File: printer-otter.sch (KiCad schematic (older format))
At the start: 52 parts, among them J1 12401610E4-2A, J3 OLED_64x32, P1 TC2030-CTX, SW1 Down, SW2 Setup, SW3 Up, U1 MT3608, U2 STM32F072C8Ux, U3 AP2204R-3.3, U4 USBLC6-4SC6, U5 L78L09_SOT89

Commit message: added connectors and board file
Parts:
- added J2: Conn_01x16, otter:Generic_FPC_0.5mm_15pin, symbol Connector_Generic:Conn_01x16
- added J4, J? (x3): Conn_01x06, Connector_Molex:Molex_PicoBlade_53261-0571_1x05-1MP_P1.25mm_Horizontal, symbol Connector_Generic:Conn_01x06
- added Q1, Q3: Q_NMOS_GSD, Package_TO_SOT_SMD:SOT-23, symbol Device:Q_NMOS_GSD
- added Q2, Q4: Q_PMOS_GSD, Package_TO_SOT_SMD:SOT-23, symbol Device:Q_PMOS_GSD
- added R11, R12, R13, R6, R7, R8: 2k, Resistor_SMD:R_0402_1005Metric, symbol Device:R
- C1, C19: value 1.0μF 25V -> 1uF; footprint Capacitor_SMD:C_0603_1608Metric -> Capacitor_SMD:C_0402_1005Metric
- C11, C9: value 1μF -> 1uF; footprint Capacitor_SMD:C_0603_1608Metric -> Capacitor_SMD:C_0402_1005Metric
- C2: value 2.2μF -> 1uF; footprint Capacitor_SMD:C_0603_1608Metric -> Capacitor_SMD:C_0402_1005Metric
- C3: value 1.0μF 25V -> 0.1μF; footprint Capacitor_SMD:C_0603_1608Metric -> Capacitor_SMD:C_0402_1005Metric
- C7: value 0.1μF -> 1uF
- D2: renamed from D?; footprint (none) -> Diode_SMD:D_SMB
- J3: footprint Connector_Harwin:Harwin_M20-89014xx_1x14_P2.54mm_Horizontal -> otter:0.69OLED
- L1: footprint (none) -> Inductor_SMD:L_Taiyo-Yuden_MD-4040
- P1: footprint Tag-Connect:TC2030-NL_SMALL -> Connector:Tag-Connect_TC2030-IDC-NL_2x03_P1.27mm_Vertical
- R15, R17: value 2kΩ -> 2k
- R4, R5: footprint (none) -> Resistor_SMD:R_0402_1005Metric
- U1: footprint (none) -> Package_TO_SOT_SMD:SOT-23-6
- U4: value USBLC6-4SC6 -> USBLC6-2SC6
- U6, U7: renamed from U?; footprint (none) -> Package_SO:SOIC-16W_5.3x10.2mm_P1.27mm
- gave numbers to parts that had none: 4
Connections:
- net labels added: +3.3V, DCLK, DCLK_HV, F3_HV, F5_HV
- net labels removed: CC1, CC2, DCLCK, S6_HV
- wire segments 161 -> 182
- no-connect marks 10 -> 13
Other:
- moved on the sheet: C10, C12, C13, C14, C15, C16, C17, C18, C20, C4, C5, C6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

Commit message: updated schematic, removed display and tag connect, routed board (80%)
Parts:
- removed C10, C12, C17, C3, C8: 0.1μF, Capacitor_SMD:C_0402_1005Metric, symbol Device:C
- removed C13, C14, C15, C16, C9: 1uF, Capacitor_SMD:C_0402_1005Metric, symbol Device:C
- removed J1: 12401610E4-2A, Connector_USB:USB_C_Receptacle_Amphenol_12401548E4-2A, symbol Connector:USB_C_Receptacle
- removed J3: OLED_64x32, otter:0.69OLED, symbol Connector_Generic:Conn_01x14
- removed J4, J? (x3): Conn_01x06, Connector_Molex:Molex_PicoBlade_53261-0571_1x05-1MP_P1.25mm_Horizontal, symbol Connector_Generic:Conn_01x06
- removed P1: TC2030-CTX, Connector:Tag-Connect_TC2030-IDC-NL_2x03_P1.27mm_Vertical, symbol Connector_Generic:Conn_02x03_Counter_Clockwise
- removed R15, R17: 2k, Resistor_SMD:R_0402_1005Metric, symbol Device:R
- removed R16: 560k, Resistor_SMD:R_0402_1005Metric, symbol Device:R_Small
- removed SW2: Setup, Button_Switch_SMD:SW_SPST_EVQP7C, symbol Switch:SW_Push
- removed SW3: Up, Button_Switch_SMD:SW_SPST_EVQP7C, symbol Switch:SW_Push
- added J1: USB, badgelib:USB-C 16Pin, symbol Connector:USB_C_Receptacle_USB2.0
- added J4: Encoder, Connector_PinHeader_2.54mm:PinHeader_1x05_P2.54mm_Vertical, symbol Connector_Generic:Conn_01x05
- added J5: UART, Connector_PinHeader_2.54mm:PinHeader_1x05_P2.54mm_Vertical, symbol Connector_Generic:Conn_01x05
- added J6: Analog, Connector_PinHeader_2.54mm:PinHeader_1x05_P2.54mm_Vertical, symbol Connector_Generic:Conn_01x05
- D2: footprint Diode_SMD:D_SMB -> Diode_SMD:D_SOD-123
- J2: value Conn_01x16 -> Printer
- U4: value USBLC6-2SC6 -> USBLC6-4SC6
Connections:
- net labels removed: INPUT0, INPUT1, INPUT2
- wire segments 182 -> 128
- no-connect marks 13 -> 4
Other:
- moved on the sheet: C11, C7, D1, D4, R1, R10, R3, R9

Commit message: schematic cleanup
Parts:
- U6, U7: footprint Package_SO:SOIC-16W_5.3x10.2mm_P1.27mm -> Package_SO:SOIC-16_3.9x9.9mm_P1.27mm
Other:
- moved on the sheet: C1, C11, C18, C19, C2, C20, C4, C5, C6, C7, D2, J1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

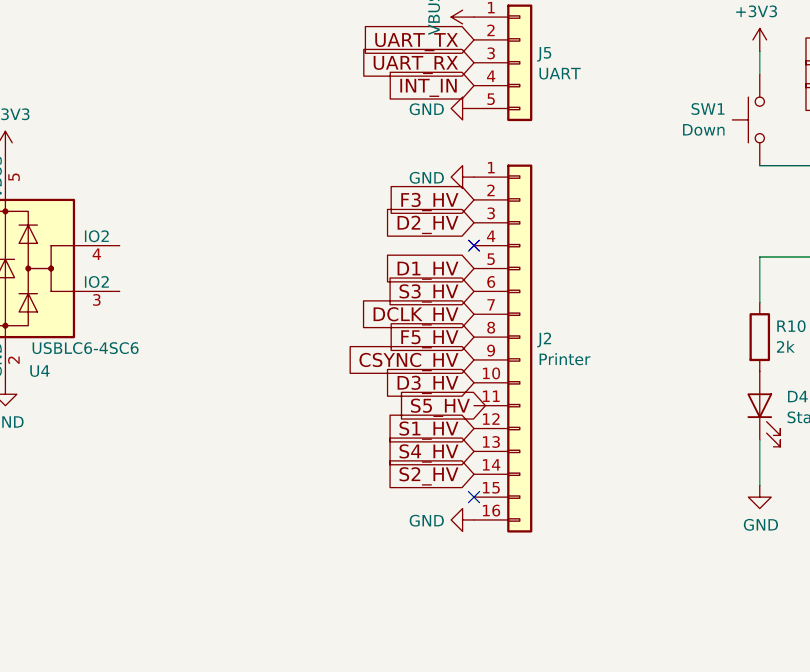
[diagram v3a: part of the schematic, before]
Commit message: fixed FPC pinout
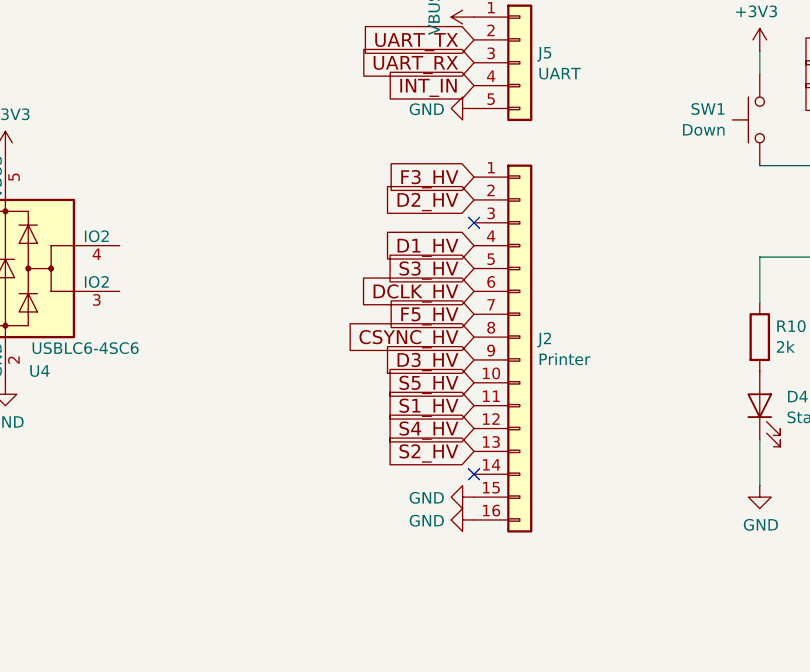
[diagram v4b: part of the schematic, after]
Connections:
- net CSYNC_HV: now also J2.8 (Pin_8); no longer J2.9 (Pin_9)
- net D1_HV: now also J2.4 (Pin_4); no longer J2.5 (Pin_5)
- net D2_HV: now also J2.2 (Pin_2); no longer J2.3 (Pin_3)
- net D3_HV: now also J2.9 (Pin_9); no longer J2.10 (Pin_10)
- net DCLK_HV: now also J2.6 (Pin_6); no longer J2.7 (Pin_7)
- net F3_HV: now also J2.1 (Pin_1); no longer J2.2 (Pin_2)
- net F5_HV: now also J2.7 (Pin_7); no longer J2.8 (Pin_8)
- net GND: now also J2.15 (Pin_15); no longer J2.1 (Pin_1)
- net S1_HV: now also J2.11 (Pin_11); no longer J2.12 (Pin_12)
- net S2_HV: now also J2.13 (Pin_13); no longer J2.14 (Pin_14)
- net S3_HV: now also J2.5 (Pin_5); no longer J2.6 (Pin_6)
- net S4_HV: now also J2.12 (Pin_12); no longer J2.13 (Pin_13)
- net S5_HV: now also J2.10 (Pin_10)
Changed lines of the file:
@@
 Text GLabel 12600 1650 3    60   Input ~ 0
 F5_HV
+Text GLabel 4250 5700 0    60   Input ~ 0
+S1_HV
+Text GLabel 4250 5900 0    60   Input ~ 0
+S2_HV
+Text GLabel 4250 5100 0    60   Input ~ 0
+S3_HV
 Text GLabel 4250 5800 0    60   Input ~ 0
-S1_HV
-Text GLabel 4250 6000 0    60   Input ~ 0
-S2_HV
+S4_HV
+Text GLabel 4250 5600 0    60   Input ~ 0
+S5_HV
 Text GLabel 4250 5200 0    60   Input ~ 0
-S3_HV
-Text GLabel 4250 5900 0    60   Input ~ 0
-S4_HV
-Text GLabel 4300 5700 0    60   Input ~ 0
-S5_HV
-Text GLabel 4250 5300 0    60   Input ~ 0
 DCLK_HV
-Text GLabel 4250 5100 0    60   Input ~ 0
+Text GLabel 4250 5000 0    60   Input ~ 0
 D1_HV
-Text GLabel 4250 4900 0    60   Input ~ 0
+Text GLabel 4250 4800 0    60   Input ~ 0
 D2_HV
-Text GLabel 4250 5600 0    60   Input ~ 0
+Text GLabel 4250 5500 0    60   Input ~ 0
 D3_HV
-Text GLabel 4250 5500 0    60   Input ~ 0
+Text GLabel 4250 5400 0    60   Input ~ 0
 CSYNC_HV
 $Comp
 L power:GND #PWR0155
 U 1 1 5C893C32
-P 4250 4700
-F 0 "#PWR0155" H 4250 4450 50  0001 C CNN
-F 1 "GND" V 4255 4572 50  0000 R CNN
-F 2 "" H 4250 4700 50  0001 C CNN
-F 3 "" H 4250 4700 50  0001 C CNN
-	1    4250 4700
+P 4250 6100
+F 0 "#PWR0155" H 4250 5850 50  0001 C CNN
+F 1 "GND" V 4255 5972 50  0000 R CNN
+F 2 "" H 4250 6100 50  0001 C CNN
+F 3 "" H 4250 6100 50  0001 C CNN
+	1    4250 6100
 	0    1    1    0
 $EndComp
-Text GLabel 4250 5400 0    60   Input ~ 0
+Text GLabel 4250 5300 0    60   Input ~ 0
 F5_HV
-Text GLabel 4250 4800 0    60   Input ~ 0
+Text GLabel 4250 4700 0    60   Input ~ 0
 F3_HV
-NoConn ~ 4250 5000
-NoConn ~ 4250 6100
+NoConn ~ 4250 4900
+NoConn ~ 4250 6000
 $Comp
 L Device:C C?

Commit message: updated kicad files
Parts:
- removed C19: 1uF, Capacitor_SMD:C_0402_1005Metric, symbol Device:C
- removed JP1: Boot, Jumper:SolderJumper-2_P1.3mm_Open_RoundedPad1.0x1.5mm, symbol Jumper:SolderJumper_2_Open
- added C3: 10µF, Capacitor_SMD:CP_Elec_4x3, symbol Device:CP1
- C1, C18, C2, C21, C22, C23, C24, C4, C5, C6, C7: footprint Capacitor_SMD:C_0402_1005Metric -> Capacitor_SMD:C_0603_1608Metric
- C11, C20: footprint Capacitor_SMD:C_0402_1005Metric -> Capacitor_SMD:C_0805_2012Metric
- R1, R10, R11, R12, R13, R2, R3, R4, R5, R6, R7, R8, R9: footprint Resistor_SMD:R_0402_1005Metric -> Resistor_SMD:R_0603_1608Metric
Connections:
- net labels added: BTN
- net labels removed: OLED_SCL, OLED_SDA
- wire segments 128 -> 132

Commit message: updated Kicad files
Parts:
- removed J6: Analog, Connector_PinHeader_2.54mm:PinHeader_1x05_P2.54mm_Vertical, symbol Connector_Generic:Conn_01x05
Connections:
- net labels added: LED_Power, LED_Status
- wire segments 132 -> 130
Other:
- moved on the sheet: D1, D4, R10, R9
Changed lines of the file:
@@
 L power:GND #PWR0117
 U 1 1 5A9ADBA9
-P 5500 6050
-F 0 "#PWR0117" H 5500 5800 50  0001 C CNN
-F 1 "GND" H 5505 5877 50  0000 C CNN
-F 2 "" H 5500 6050 50  0001 C CNN
-F 3 "" H 5500 6050 50  0001 C CNN
-	1    5500 6050
+P 5250 6500
+F 0 "#PWR0117" H 5250 6250 50  0001 C CNN
+F 1 "GND" H 5255 6327 50  0000 C CNN
+F 2 "" H 5250 6500 50  0001 C CNN
+F 3 "" H 5250 6500 50  0001 C CNN
+	1    5250 6500
 	1    0    0    -1
 $EndComp
@@
 L Device:LED D4
 U 1 1 5A9BB5C1
-P 5500 5700
-F 0 "D4" V 5538 5583 50  0000 R CNN
-F 1 "Status" V 5447 5583 50  0000 R CNN
-F 2 "LED_SMD:LED_0603_1608Metric" H 5500 5700 50  0001 C CNN
-F 3 "~" H 5500 5700 50  0001 C CNN
-	1    5500 5700
+P 5250 6150
+F 0 "D4" V 5288 6033 50  0000 R CNN
+F 1 "Status" V 5197 6033 50  0000 R CNN
+F 2 "LED_SMD:LED_0603_1608Metric" H 5250 6150 50  0001 C CNN
+F 3 "~" H 5250 6150 50  0001 C CNN
+	1    5250 6150
 	0    -1   -1   0
 $EndComp
@@
 L power:GND #PWR0129
 U 1 1 5BDFFE89
-P 6000 6050
-F 0 "#PWR0129" H 6000 5800 50  0001 C CNN
-F 1 "GND" H 6005 5877 50  0000 C CNN
-F 2 "" H 6000 6050 50  0001 C CNN
-F 3 "" H 6000 6050 50  0001 C CNN
-	1    6000 6050
+P 5750 6500
+F 0 "#PWR0129" H 5750 6250 50  0001 C CNN
+F 1 "GND" H 5755 6327 50  0000 C CNN
+F 2 "" H 5750 6500 50  0001 C CNN
+F 3 "" H 5750 6500 50  0001 C CNN
+	1    5750 6500
 	1    0    0    -1
 $EndComp
@@
 L Device:LED D1
 U 1 1 5BDFFE8F
-P 6000 5700
-F 0 "D1" V 6038 5583 50  0000 R CNN
-F 1 "Power" V 5947 5583 50  0000 R CNN
-F 2 "LED_SMD:LED_0603_1608Metric" H 6000 5700 50  0001 C CNN
-F 3 "~" H 6000 5700 50  0001 C CNN
-	1    6000 5700
+P 5750 6150
+F 0 "D1" V 5788 6033 50  0000 R CNN
+F 1 "Power" V 5697 6033 50  0000 R CNN
+F 2 "LED_SMD:LED_0603_1608Metric" H 5750 6150 50  0001 C CNN
+F 3 "~" H 5750 6150 50  0001 C CNN
+	1    5750 6150
 	0    -1   -1   0
 $EndComp
@@
 L Device:R R9
 U 1 1 5BDFFE96
-P 6000 5400
-F 0 "R9" H 6070 5446 50  0000 L CNN
-F 1 "2k" H 6070 5355 50  0000 L CNN
-F 2 "Resistor_SMD:R_0603_1608Metric" V 5930 5400 50  0001 C CNN
-F 3 "~" H 6000 5400 50  0001 C CNN
-	1    6000 5400
+P 5750 5850
+F 0 "R9" H 5820 5896 50  0000 L CNN
+F 1 "2k" H 5820 5805 50  0000 L CNN
+F 2 "Resistor_SMD:R_0603_1608Metric" V 5680 5850 50  0001 C CNN
+F 3 "~" H 5750 5850 50  0001 C CNN
+	1    5750 5850
 	1    0    0    -1
 $EndComp
@@
 L Device:R R10
 U 1 1 5A9BB9B4
-P 5500 5400
-F 0 "R10" H 5570 5446 50  0000 L CNN
-F 1 "2k" H 5570 5355 50  0000 L CNN
-F 2 "Resistor_SMD:R_0603_1608Metric" V 5430 5400 50  0001 C CNN
-F 3 "~" H 5500 5400 50  0001 C CNN
-	1    5500 5400
-	1    0    0    -1
-$EndComp
-Wire Wire Line
-	6000 5850 6000 6050
-Wire Wire Line
-	5500 5850 5500 6050
+P 5250 5850
+F 0 "R10" H 5320 5896 50  0000 L CNN
+F 1 "2k" H 5320 5805 50  0000 L CNN
+F 2 "Resistor_SMD:R_0603_1608Metric" V 5180 5850 50  0001 C CNN
+F 3 "~" H 5250 5850 50  0001 C CNN
+	1    5250 5850
+	1    0    0    -1
+$EndComp
+Wire Wire Line
+	5750 6300 5750 6500
+Wire Wire Line
+	5250 6300 5250 6500
 $Comp
 L MCU_ST_STM32F0:STM32F072C8Ux U2
@@
 Text GLabel 7750 3850 2    60   Input ~ 0
 DCLK
+Text GLabel 7750 4350 2    60   Input ~ 0
+S1
+Text GLabel 7750 4150 2    60   Input ~ 0
+S2
+Text GLabel 7750 3950 2    60   Input ~ 0
+S3
+Text GLabel 7750 4250 2    60   Input ~ 0
+S4
+Text GLabel 7750 4050 2    60   Input ~ 0
+S5
 Text GLabel 7750 4550 2    60   Input ~ 0
-S1
-Text GLabel 7750 4050 2    60   Input ~ 0
-S2
-Text GLabel 7750 4150 2    60   Input ~ 0
-S3
+F3
 Text GLabel 7750 4450 2    60   Input ~ 0
-S4
-Text GLabel 7750 3950 2    60   Input ~ 0
-S5
-Text GLabel 7750 4350 2    60   Input ~ 0
-F3
-Text GLabel 7750 4250 2    60   Input ~ 0
 F5
 Text GLabel 6450 4050 0    60   Input ~ 0
@@
 	0    1    1    0
 $EndComp
-Text GLabel 4250 2700 0    60   Input ~ 0
-GPIO_ANALOG0
-Text GLabel 4250 2800 0    60   Input ~ 0
-GPIO_ANALOG1
-Text GLabel 4250 2900 0    60   Input ~ 0
-GPIO_ANALOG2
-$Comp
-L power:+3.3V #PWR0158
-U 1 1 5C9A9260
-P 4250 2600
-F 0 "#PWR0158" H 4250 2450 50  0001 C CNN
-F 1 "+3.3V" V 4265 2728 50  0000 L CNN
-F 2 "" H 4250 2600 50  0001 C CNN
-F 3 "" H 4250 2600 50  0001 C CNN
-	1    4250 2600
-	0    -1   -1   0
-$EndComp
 $Comp
 L power:GND #PWR0163
@@
 $EndComp
 $Comp
-L Connector_Generic:Conn_01x05 J6
-U 1 1 5C767F1F
-P 4450 2800
-F 0 "J6" H 4529 2842 50  0000 L CNN
-F 1 "Analog" H 4529 2751 50  0000 L CNN
-F 2 "Connector_PinHeader_2.54mm:PinHeader_1x05_P2.54mm_Vertical" H 4450 2800 50  0001 C CNN
-F 3 "~" H 4450 2800 50  0001 C CNN
-	1    4450 2800
-	1    0    0    -1
-$EndComp
-$Comp
-L power:GND #PWR0157
-U 1 1 5C9A9169
-P 4250 3000
-F 0 "#PWR0157" H 4250 2750 50  0001 C CNN
-F 1 "GND" V 4255 2872 50  0000 R CNN
-F 2 "" H 4250 3000 50  0001 C CNN
-F 3 "" H 4250 3000 50  0001 C CNN
-	1    4250 3000
-	0    1    1    0
-$EndComp
-$Comp
 L Connector:USB_C_Receptacle_USB2.0 J1
 U 1 1 5C7ADF63
@@
 	6800 1250 6900 1250
 Wire Wire Line
-	6450 5150 6000 5150
-Wire Wire Line
-	6000 5150 6000 5250
-Wire Wire Line
-	6450 5050 5500 5050
-Wire Wire Line
-	5500 5050 5500 5250
+	5750 5600 5750 5700
+Wire Wire Line
+	5250 5500 5250 5700
 Wire Wire Line
 	8450 1250 8900 1250
@@
 Wire Wire Line
 	5550 2950 6450 2950
+Text GLabel 5750 5600 1    60   Input ~ 0
+LED_Power
+Text GLabel 5250 5500 1    60   Input ~ 0
+LED_Status
+Text GLabel 6450 3850 0    60   Input ~ 0
+LED_Status
+Text GLabel 6450 3950 0    60   Input ~ 0
+LED_Power
 $EndSCHEMATC
